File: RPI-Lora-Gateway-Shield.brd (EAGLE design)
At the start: 99.1 x 99.1 mm, 60 parts, among them J1 GROVE, J10 CON_TERMINAL_BLOCK_02-5MM, J11 JUMPER_1X30805, J12 JUMPER_1X30805, J13 GROVE I2C, J14 2.54_I2C, J15 POWER_JACKPTH, J4 RASPBERRYPI-40-PIN-GPIO, J5 DHTxx, J6 2.54_I2C, J7 2.54_I2C, J8 CON_TERMINAL_BLOCK_02-5MM, J9 CON_TERMINAL_BLOCK_02-5MM

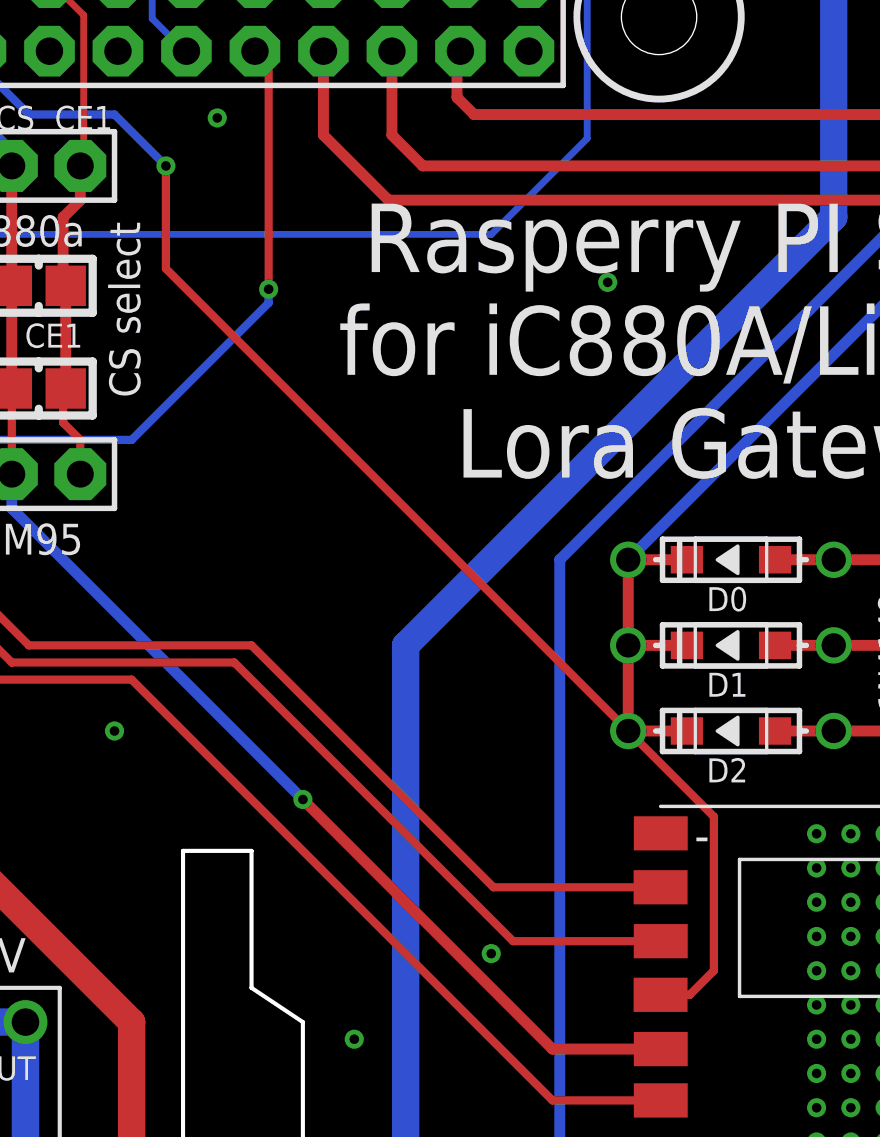
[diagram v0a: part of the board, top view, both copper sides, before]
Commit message: Routing Overlap fix
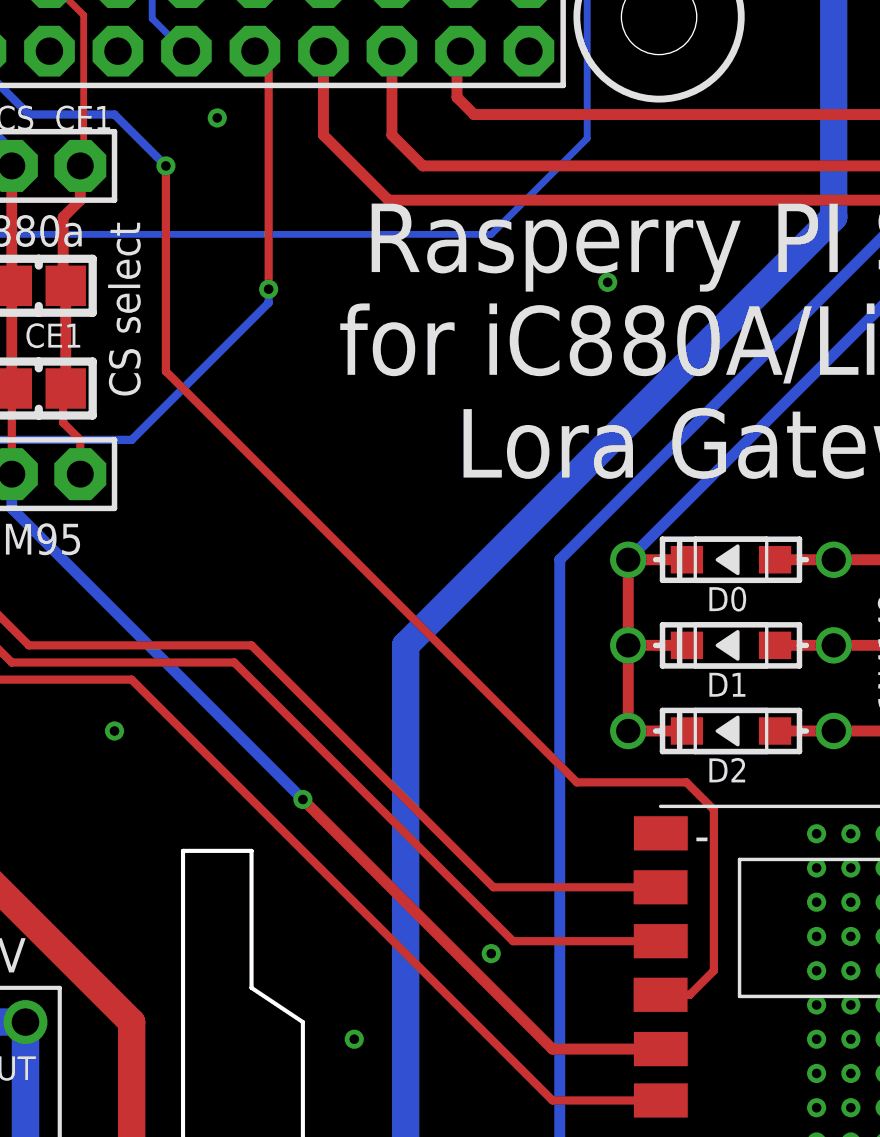
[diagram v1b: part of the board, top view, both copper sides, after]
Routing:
- net SPI_SCLK: track 60.4 -> 62.8 mm
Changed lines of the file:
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@@
 <wire x1="52.705" y1="70.485" x2="54.61" y2="68.58" width="0.3048" layer="16"/>
 <via x="54.61" y="68.58" extent="1-16" drill="0.3556" diameter="0.7112"/>
-<wire x1="54.61" y1="68.58" x2="54.61" y2="64.77" width="0.3048" layer="1"/>
-<wire x1="54.61" y1="64.77" x2="74.93" y2="44.45" width="0.3048" layer="1"/>
-<wire x1="74.93" y1="44.45" x2="74.93" y2="38.735" width="0.3048" layer="1"/>
+<wire x1="74.93" y1="44.704" x2="74.93" y2="38.735" width="0.3048" layer="1"/>
 <wire x1="74.93" y1="38.735" x2="74.0372" y2="37.8422" width="0.3048" layer="1"/>
 <wire x1="72.955" y1="37.8422" x2="74.0372" y2="37.8422" width="0.3048" layer="1"/>
+<wire x1="74.93" y1="44.704" x2="73.914" y2="45.72" width="0.3048" layer="1"/>
+<wire x1="73.914" y1="45.72" x2="69.85" y2="45.72" width="0.3048" layer="1"/>
+<wire x1="69.85" y1="45.72" x2="54.61" y2="60.96" width="0.3048" layer="1"/>
+<wire x1="54.61" y1="60.96" x2="54.61" y2="68.58" width="0.3048" layer="1"/>
 </signal>
 <signal name="GND">

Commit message: Bump to Version 1.1
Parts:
- removed GROVE: GROVE I2C, Connector -2016:HW4-2.0
- removed H5, H6: STAND-OFF, SparkFun-Electromechanical:STAND-OFF
- removed J$1: ANTENNATINY, _c2h:SMA_UFL_PAD_TINY
- added H8, H9: STAND-OFF, SparkFun-Electromechanical:STAND-OFF
- added J16: 2.54_PWR, _c2h:1X04_NO_LOCK
- added U$3: ANTENNA-UFL, _c2h:UFL_PAD
- added U$8: DC-BREAKOUTFIXED, _c2h:DC-DC-FIXED
- JP1, JP2: device microbuilder:JUMPER3 -> microbuilder:JUMPER2
- moved H3 111.4 mm to (94.2, 5.97)
- moved H2 101.3 mm to (49.5, 96.0)
- moved H1 88.4 mm to (4.83, 5.97)
- moved R10 73.1 mm to (86.4, 91.4), turned to 90 degrees
- moved R5 73.1 mm to (86.4, 91.4), turned to 270 degrees
- moved U$9 69.9 mm to (27.9, 91.4)
- moved J5 69.2 mm to (94.0, 84.5), turned to 270 degrees
- moved JP2 52.5 mm to (7.62, 24.8), turned to 270 degrees
- moved J14 49.5 mm to (68.6, 90.8), turned to 90 degrees
- moved H4 45.1 mm to (49.5, 3.56)
- moved JP1 43.0 mm to (8.26, 82.5), turned to 270 degrees
- moved J7 42.6 mm to (61.6, 90.8), turned to 90 degrees
- moved J6 39.1 mm to (57.8, 90.8), turned to 90 degrees
- moved R11 31.2 mm to (73.0, 55.2), turned to 90 degrees
- moved R12 31.2 mm to (73.0, 55.2), turned to 90 degrees
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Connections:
- removed net N$14: D3.A, D4.2, J15.PWR, J8.1
- new net 5V-PI: J4.2, J4.4, JP1.2
- new net SPI_SEL: J12.2, U$2.NSS
- new net VIN: D3.A, D4.2, J15.PWR, J16.2, J16.3, J8.1, JP2.1
- net +5V: now also J16.4, JP1.1, JP2.2, U$8.VOUT-1, U$8.VOUT-2; no longer J4.2, J4.4
- net 3V3: no longer GROVE.3, R11.P$1, R12.1
- net GND: now also J16.1, R11.P$1, R12.1, U$3.GND1, U$3.GND2, U$8.GND-1, U$8.GND-2, U$8.GND-3, U$8.GND-4; no longer GROVE.4, J$1.GND1, J$1.GND2, J$1.GND3, J$1.GND4
- net N$28: now also U$8.VIN-1, U$8.VIN-2
- net N$29: now also U$3.ANT1, U$3.ANT2; no longer J$1.ANT1, J$1.ANT2, J$1.ANT3
- net SCL: no longer GROVE.1
- net SDA: no longer GROVE.2
- net SPI_CE0: no longer JP1.1, JP2.1
- net SPI_CE1: no longer JP1.3, JP2.3
- net SPI_SS: no longer J12.2, JP1.2, JP2.2, U$2.NSS
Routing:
- net VIN: track 0.00 -> 65.5 mm
- net SDA: track 150.2 -> 195.8 mm
- net SPI_SS: track 68.2 -> 27.6 mm
- net N$27: track 61.7 -> 23.0 mm
- net N$14: track 38.2 -> 0.00 mm
- net N$26: track 57.3 -> 25.9 mm
- net SCL: track 137.0 -> 168.1 mm
- net GPIO19: track 112.0 -> 81.5 mm
- net GPIO35: track 100.9 -> 73.6 mm
- net SPI_SEL: track 0.00 -> 26.9 mm, vias 0 -> 2
- net 3V3: track 353.9 -> 327.9 mm
- net N$16: track 54.6 -> 29.6 mm, vias 1 -> 0
- net GPIO24: track 18.2 -> 39.5 mm, vias 0 -> 1
- net 5V-PI: track 0.00 -> 19.4 mm
- net +5V: track 174.4 -> 157.0 mm
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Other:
- outline, holes or cut-outs redrawn
- board text added: "Antenna Fix"
- board text added: "Close JP1 to share power between PI and ic880a"
- board text added: "Close JP2 if power supply is 5V and not using DC/DC"
- board text added: "DC Barel"
- board text added: "V1.1"
- board text removed: "CE0"
- board text removed: "CE1"
- board text removed: "CS"
- board text removed: "DC Barel Jack"
- board text removed: "V1.0"

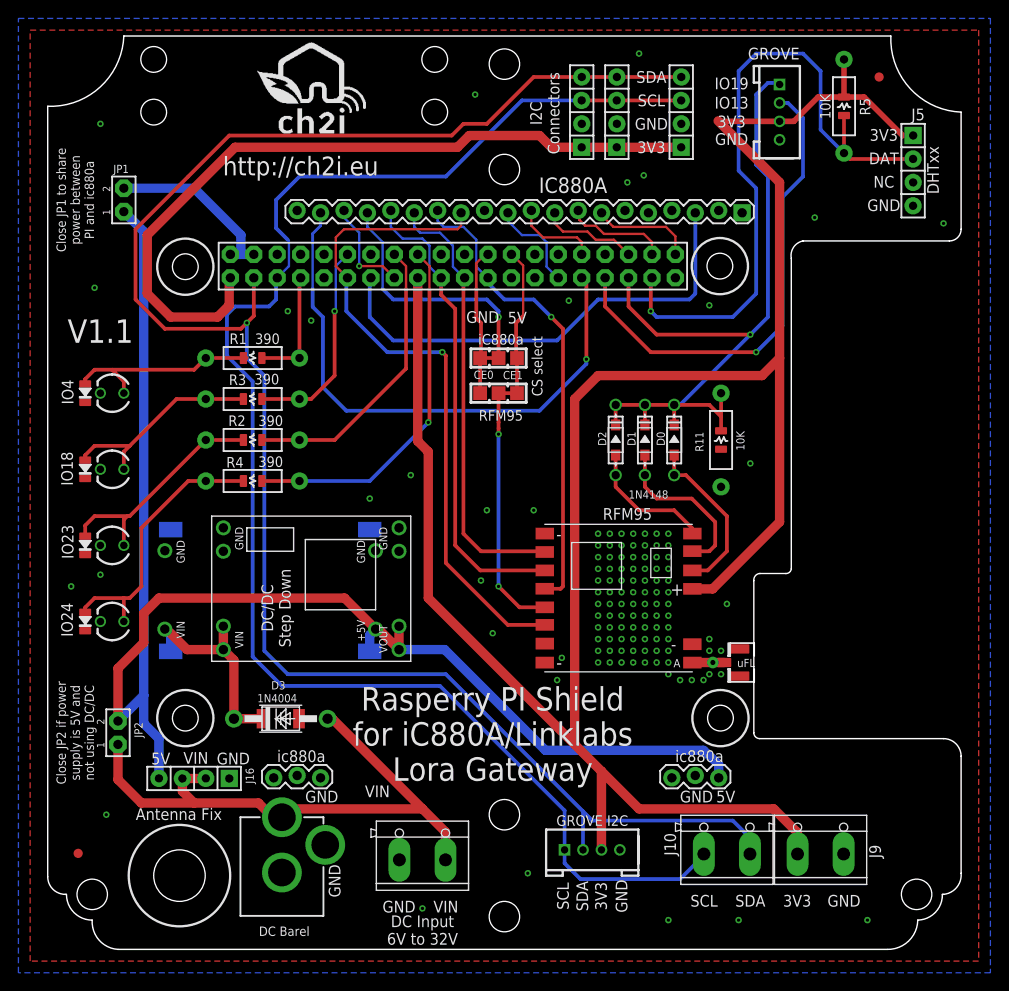
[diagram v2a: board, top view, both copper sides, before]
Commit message: Minor Silk and Trace Fix
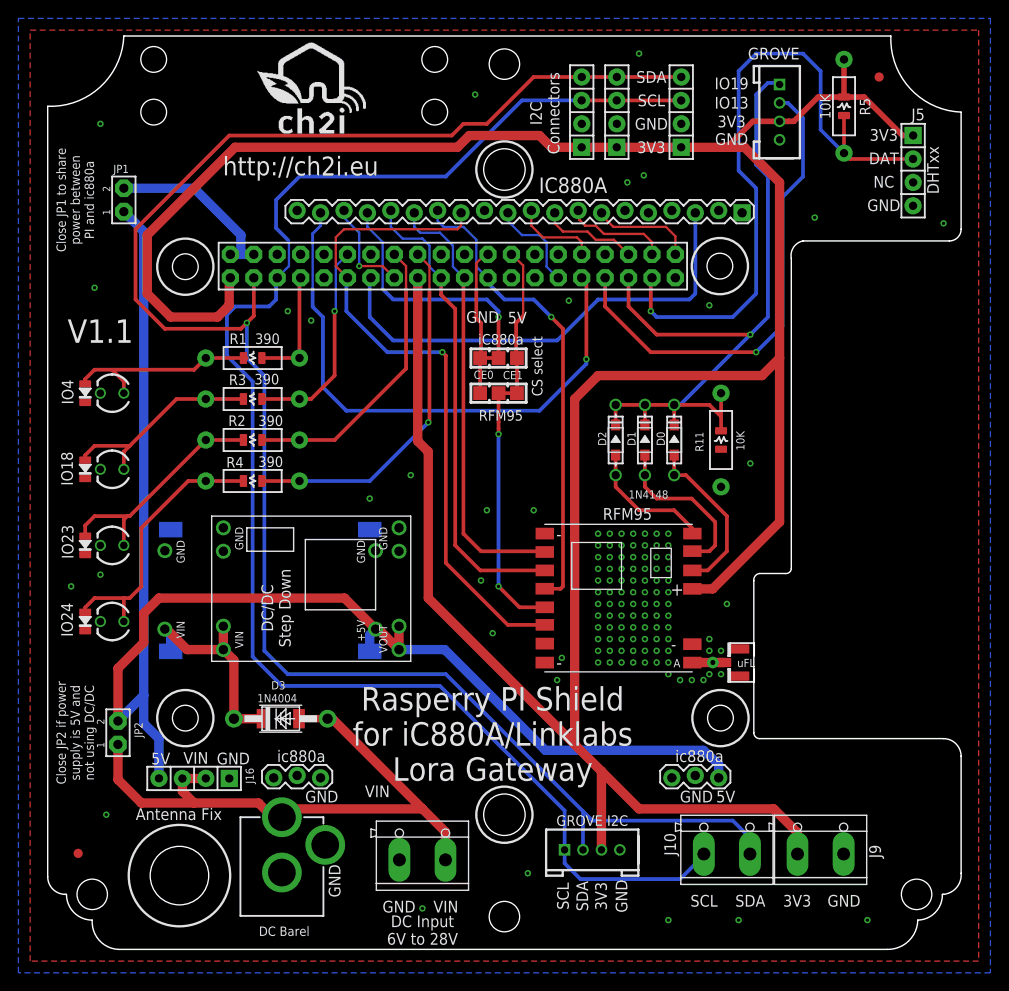
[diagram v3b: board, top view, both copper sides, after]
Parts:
- removed H8, H9: STAND-OFF, SparkFun-Electromechanical:STAND-OFF
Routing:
- net VIN: track 65.5 -> 68.6 mm
- net 3V3: track 327.9 -> 331.0 mm
- net GPIO19: track 81.5 -> 82.2 mm
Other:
- board text added: "DC Input 6V to 28V"
- board text removed: "DC Input 6V to 32V"
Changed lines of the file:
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@@
 <setting verticaltext="up"/>
 </settings>
-<grid distance="25" unitdist="mil" unit="mil" style="dots" multiple="1" display="yes" altdistance="5" altunitdist="mil" altunit="mil"/>
+<grid distance="25" unitdist="mil" unit="mil" style="dots" multiple="1" display="yes" altdistance="2.5" altunitdist="mil" altunit="mil"/>
 <layers>
 <layer number="1" name="Top" color="4" fill="1" visible="yes" active="yes"/>
@@
 <text x="38.1" y="4.6355" size="1.27" layer="21" font="vector" ratio="15" rot="R180" align="center">GND</text>
 <text x="40.64" y="2.0955" size="1.27" layer="21" font="vector" ratio="15" rot="R180" align="center">DC Input
-6V to 32V</text>
+6V to 28V</text>
 <text x="90.678" y="88.3285" size="1.27" layer="21" font="vector" ratio="15" align="center">3V3</text>
 <text x="90.678" y="85.7885" size="1.27" layer="21" font="vector" ratio="15" align="center">DAT</text>
@@
 <wire x1="99.06" y1="8.255" x2="97.155" y2="5.969" width="0.1524" layer="20" curve="-90"/>
 <wire x1="94.361" y1="3.175" x2="91.059" y2="0" width="0.1524" layer="20" curve="-90"/>
-<hole x="14.2875" y="8.001" drill="5.588"/>
+<hole x="14.2875" y="8.001" drill="6.35"/>
 <circle x="14.2875" y="8.001" radius="5.5" width="0.254" layer="21"/>
 <text x="14.224" y="14.6685" size="1.27" layer="21" font="vector" ratio="15" rot="R180" align="center">Antenna Fix</text>
@@
 <hole x="11.4935" y="96.52" drill="2.794"/>
 <hole x="41.9735" y="96.52" drill="2.794"/>
+<hole x="49.53" y="14.605" drill="4.5"/>
+<hole x="49.53" y="84.582" drill="4.5"/>
+<circle x="49.53" y="14.605" radius="3.048" width="0.254" layer="21"/>
+<circle x="49.53" y="84.582" radius="3.048" width="0.254" layer="21"/>
 </plain>
 <attributes>
@@
 </element>
 <element name="U$8" library="_c2h" package="DC-DC-FIXED" value="DC-BREAKOUTFIXED" x="22.225" y="39.0525" smashed="yes" rot="MR180"/>
-<element name="H8" library="SparkFun-Electromechanical" package="STAND-OFF" value="STAND-OFF" x="49.53" y="84.582"/>
-<element name="H9" library="SparkFun-Electromechanical" package="STAND-OFF" value="STAND-OFF" x="49.53" y="14.605"/>
 <element name="H2" library="SparkFun-Electromechanical" package="STAND-OFF" value="STAND-OFF" x="49.53" y="96.012"/>
 <element name="H4" library="SparkFun-Electromechanical" package="STAND-OFF" value="STAND-OFF" x="49.53" y="3.556"/>
@@
 <contactref element="J1" pad="3"/>
 <contactref element="R10" pad="2"/>
-<wire x1="72.7075" y1="89.8525" x2="79.375" y2="83.185" width="1.016" layer="1"/>
+<wire x1="75.57135" y1="86.98865" x2="79.375" y2="83.185" width="1.016" layer="1"/>
 <wire x1="81.28" y1="10.385" x2="81.28" y2="12.7" width="1.016" layer="1"/>
 <wire x1="81.28" y1="12.7" x2="78.74" y2="15.24" width="1.016" layer="1"/>
@@
 <wire x1="77.47" y1="62.23" x2="79.375" y2="64.135" width="1.016" layer="1"/>
 <wire x1="68.58" y1="86.868" x2="68.70065" y2="86.98865" width="1.016" layer="1"/>
-<wire x1="79.375" y1="89.805" x2="72.755" y2="89.805" width="0.6096" layer="1"/>
-<wire x1="72.755" y1="89.805" x2="72.7075" y2="89.8525" width="0.6096" layer="1"/>
 <wire x1="93.85935" y1="88.27135" x2="92.70365" y2="88.27135" width="0.6096" layer="1"/>
 <wire x1="92.70365" y1="88.27135" x2="88.535" y2="92.44" width="0.6096" layer="1"/>
@@
 <wire x1="86.36" y1="92.44" x2="83.55" y2="92.44" width="0.6096" layer="1"/>
 <wire x1="83.55" y1="92.44" x2="80.915" y2="89.805" width="0.6096" layer="1"/>
-<wire x1="79.375" y1="89.805" x2="80.915" y2="89.805" width="0.6096" layer="1"/>
+<wire x1="80.375" y1="89.805" x2="80.915" y2="89.805" width="0.6096" layer="1"/>
 <wire x1="86.36" y1="96.52" x2="86.36" y2="92.44" width="0.6096" layer="1"/>
 <wire x1="10.795" y1="77.47" x2="20.32" y2="86.995" width="1.016" layer="1"/>
@@
 <wire x1="54.61" y1="86.995" x2="57.8993" y2="86.995" width="1.016" layer="1"/>
 <wire x1="57.8993" y1="86.995" x2="57.90565" y2="86.98865" width="1.016" layer="1"/>
-<wire x1="72.755" y1="89.805" x2="68.70065" y2="86.98865" width="0" layer="19" extent="1-1"/>
+<wire x1="68.70065" y1="86.98865" x2="73.66" y2="86.98865" width="1.016" layer="1"/>
+<wire x1="73.66" y1="86.98865" x2="75.57135" y2="86.98865" width="1.016" layer="1"/>
+<wire x1="79.375" y1="89.805" x2="76.47635" y2="89.805" width="0.6096" layer="1"/>
+<wire x1="76.47635" y1="89.805" x2="73.66" y2="86.98865" width="0.6096" layer="1"/>
+<wire x1="80.375" y1="89.805" x2="79.375" y2="89.805" width="0.6096" layer="1"/>
 </signal>
 <signal name="GPIO25">
@@
 <wire x1="78.105" y1="93.98" x2="79.2" y2="93.98" width="0.4064" layer="16"/>
 <wire x1="79.2" y1="93.98" x2="79.375" y2="93.805" width="0.4064" layer="16"/>
-<wire x1="67.945" y1="59.055" x2="68.58" y2="59.055" width="0" layer="19" extent="16-16"/>
+<wire x1="68.58" y1="59.055" x2="67.945" y2="59.055" width="0.4064" layer="16"/>
 </signal>
 <signal name="VIN">
@@
 <wire x1="14.605" y1="18.53565" x2="14.605" y2="17.145" width="1.016" layer="1"/>
 <wire x1="14.605" y1="17.145" x2="15.875" y2="15.875" width="1.016" layer="1"/>
-<wire x1="30.353" y1="25.019" x2="27.253" y2="25.019" width="0" layer="19" extent="1-1"/>
+<wire x1="30.353" y1="25.019" x2="27.253" y2="25.019" width="0.8128" layer="1"/>
 </signal>
 <signal name="DIO0">

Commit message: Bump to V1.2
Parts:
- added FTDI: (no value), _c2h:M1X6
- added SW1: (no value), adafruit:TACT_PANA-EVQ
- added U$11: OKI-78SR, _c2h:OKI-78SRH
- moved FID3 18.6 mm to (71.8, 97.2)
- moved JP1 7.62 mm to (8.26, 74.9)
- moved U$1 4.49 mm to (24.8, 90.8)
- moved U$9 4.49 mm to (23.5, 90.8)
- moved R10 0.90 mm to (85.7, 90.8)
- moved R5 0.90 mm to (85.7, 90.8)
- turned J5 to 90 degrees
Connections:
- net GPIO35 renamed GPIO26
- removed net N$28: D3.C, D4.1, DC/DC.VIN-1, DC/DC.VIN-2, U$8.VIN-1, U$8.VIN-2
- new net N$14: D3.C, D4.1, DC/DC.VIN-1, DC/DC.VIN-2, U$11.1, U$8.VIN-1, U$8.VIN-2
- new net RXI: FTDI.4, J4.10
- new net TXO: FTDI.5, J4.8
- net +5V: now also U$11.3
- net 3V3: now also SW1.P$2
- net GND: now also FTDI.1, U$11.2
- net GPIO19: now also SW1.P$1
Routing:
- net GPIO19: track 82.2 -> 163.2 mm, vias 1 -> 2
- net N$14: track 0.00 -> 27.9 mm
- net RXI: track 0.00 -> 26.0 mm, vias 0 -> 1
- net N$28: track 23.6 -> 0.00 mm
- net TXO: track 0.00 -> 22.4 mm, vias 0 -> 1
- net 3V3: track 331.0 -> 348.4 mm
- net +5V: track 157.0 -> 152.5 mm
- net GPIO26: track 73.6 -> 72.7 mm
- net GPIO24: track 39.5 -> 40.2 mm
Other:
- outline, holes or cut-outs redrawn
- board text added: "3.3V Only FTDI"
- board text added: "G"
- board text added: "I2C"
- board text added: "Rasperry PI shield for iC880A Lora Gateway"
- board text added: "V1.2"
- board text added: "VOUT"
- board text added: "ch2i.eu"
- board text removed: "I2C Connectors"
- board text removed: "Rasperry PI Shield for iC880A/Linklabs Lora Gateway"
- board text removed: "V1.1"
